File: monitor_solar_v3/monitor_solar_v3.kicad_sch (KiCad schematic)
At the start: 41 parts, among them J1 Panel, J10 GPIO, J11 Jumper, J2 ACS712, J3 Battery, J4 AMP_OUT, J5 JUMPER_PROG, J6 JUMPER_PROG, J7 PROGRAM, J9 Reg 5V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

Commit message: PCB V3 finished
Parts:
- added R15: 10k, Resistor_THT:R_Axial_DIN0207_L6.3mm_D2.5mm_P10.16mm_Horizontal, symbol Device:R
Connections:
- net +3.3V: now also R15.1
- net GPIO15: now also R15.2
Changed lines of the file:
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@@
 	)
 	(junction
+		(at 260.35 60.96)
+		(diameter 0)
+		(color 0 0 0 0)
+	)
+	(junction
 		(at 22.86 25.4)
 		(diameter 0)
@@
 	(wire
 		(pts
+			(xy 260.35 50.8) (xy 260.35 52.07)
+		)
+		(stroke
+			(width 0)
+			(type default)
+		)
+	)
+	(wire
+		(pts
 			(xy 49.53 134.62) (xy 49.53 132.08)
 		)
@@
 	(wire
 		(pts
-			(xy 238.76 60.96) (xy 234.95 60.96)
-		)
-		(stroke
-			(width 0)
-			(type default)
-		)
-	)
-	(wire
-		(pts
 			(xy 48.26 81.28) (xy 50.8 81.28)
 		)
@@
 	(wire
 		(pts
+			(xy 260.35 60.96) (xy 234.95 60.96)
+		)
+		(stroke
+			(width 0)
+			(type default)
+		)
+	)
+	(wire
+		(pts
 			(xy 196.85 25.4) (xy 199.39 25.4)
 		)
@@
 	(wire
 		(pts
+			(xy 260.35 59.69) (xy 260.35 60.96)
+		)
+		(stroke
+			(width 0)
+			(type default)
+		)
+	)
+	(wire
+		(pts
 			(xy 196.85 151.13) (xy 186.69 151.13)
 		)
@@
 	(wire
 		(pts
+			(xy 260.35 60.96) (xy 265.43 60.96)
+		)
+		(stroke
+			(width 0)
+			(type default)
+		)
+	)
+	(wire
+		(pts
 			(xy 22.86 45.72) (xy 25.4 45.72)
 		)
@@
 	(global_label "GPIO15"
 		(shape input)
-		(at 238.76 60.96 0)
+		(at 265.43 60.96 0)
 		(fields_autoplaced yes)
 		(effects
@@
 		)
 		(property "Intersheetrefs" "${INTERSHEET_REFS}"
-			(at 248.6395 60.96 0)
+			(at 275.3095 60.96 0)
 			(effects
 				(font
@@
 	)
 	(symbol
+		(lib_id "power:+3.3V")
+		(at 260.35 50.8 0)
+		(unit 1)
+		(exclude_from_sim no)
+		(in_bom yes)
+		(on_board yes)
+		(dnp no)
+		(fields_autoplaced yes)
+		(property "Reference" "#PWR034"
+			(at 260.35 54.61 0)
+			(effects
+				(font
+					(size 1.27 1.27)
+				)
+				(hide yes)
+			)
+		)
+		(property "Value" "+3.3V"
+			(at 260.35 45.72 0)
+			(effects
+				(font
+					(size 1.27 1.27)
+				)
+			)
+		)
+		(property "Footprint" ""
+			(at 260.35 50.8 0)
+			(effects
+				(font
+					(size 1.27 1.27)
+				)
+				(hide yes)
+			)
+		)
+		(property "Datasheet" ""
+			(at 260.35 50.8 0)
+			(effects
+				(font
+					(size 1.27 1.27)
+				)
+				(hide yes)
+			)
+		)
+		(property "Description" "Power symbol creates a global label with name \"+3.3V\""
+			(at 260.35 50.8 0)
+			(effects
+				(font
+					(size 1.27 1.27)
+				)
+				(hide yes)
+			)
+		)
+		(pin "1"
+		)
+		(instances
+			(project "monitor_solar_v3"
+				(path "/d4e2a079-328a-41d5-a5a0-7716b5883be5"
+					(reference "#PWR034")
+					(unit 1)
+				)
+			)
+		)
+	)
+	(symbol
 		(lib_id "power:GND")
 		(at 186.69 156.21 0)
@@
 					(unit 1)
 				)
+			)
+		)
+	)
+	(symbol
+		(lib_id "Device:R")
+		(at 260.35 55.88 0)
+		(unit 1)
+		(exclude_from_sim no)
+		(in_bom yes)
+		(on_board yes)
+		(dnp no)
+		(fields_autoplaced yes)
+		(property "Reference" "R15"
+			(at 262.89 54.6099 0)
+			(effects
+				(font
+					(size 1.27 1.27)
+				)
+				(justify left)
+			)
+		)
+		(property "Value" "10k"
+			(at 262.89 57.1499 0)
+			(effects
+				(font
+					(size 1.27 1.27)
+				)
+				(justify left)
+			)
+		)
+		(property "Footprint" "Resistor_THT:R_Axial_DIN0207_L6.3mm_D2.5mm_P10.16mm_Horizontal"
+			(at 258.572 55.88 90)
+			(effects
+				(font
+					(size 1.27 1.27)
+				)
+				(hide yes)
+			)
+		)
+		(property "Datasheet" "~"
+			(at 260.35 55.88 0)
+			(effects
+				(font
+					(size 1.27 1.27)
+				)
+				(hide yes)
+			)
+		)
+		(property "Description" "Resistor"
+			(at 260.35 55.88 0)
+			(effects
+				(font
+					(size 1.27 1.27)
+				)
+				(hide yes)
+			)
+		)
+		(pin "1"
+		)
+		(pin "2"
+		)
+		(instances
+			(project "monitor_solar_v3"
+				(path "/d4e2a079-328a-41d5-a5a0-7716b5883be5"
+					(reference "R15")
+					(unit 1)
+				)

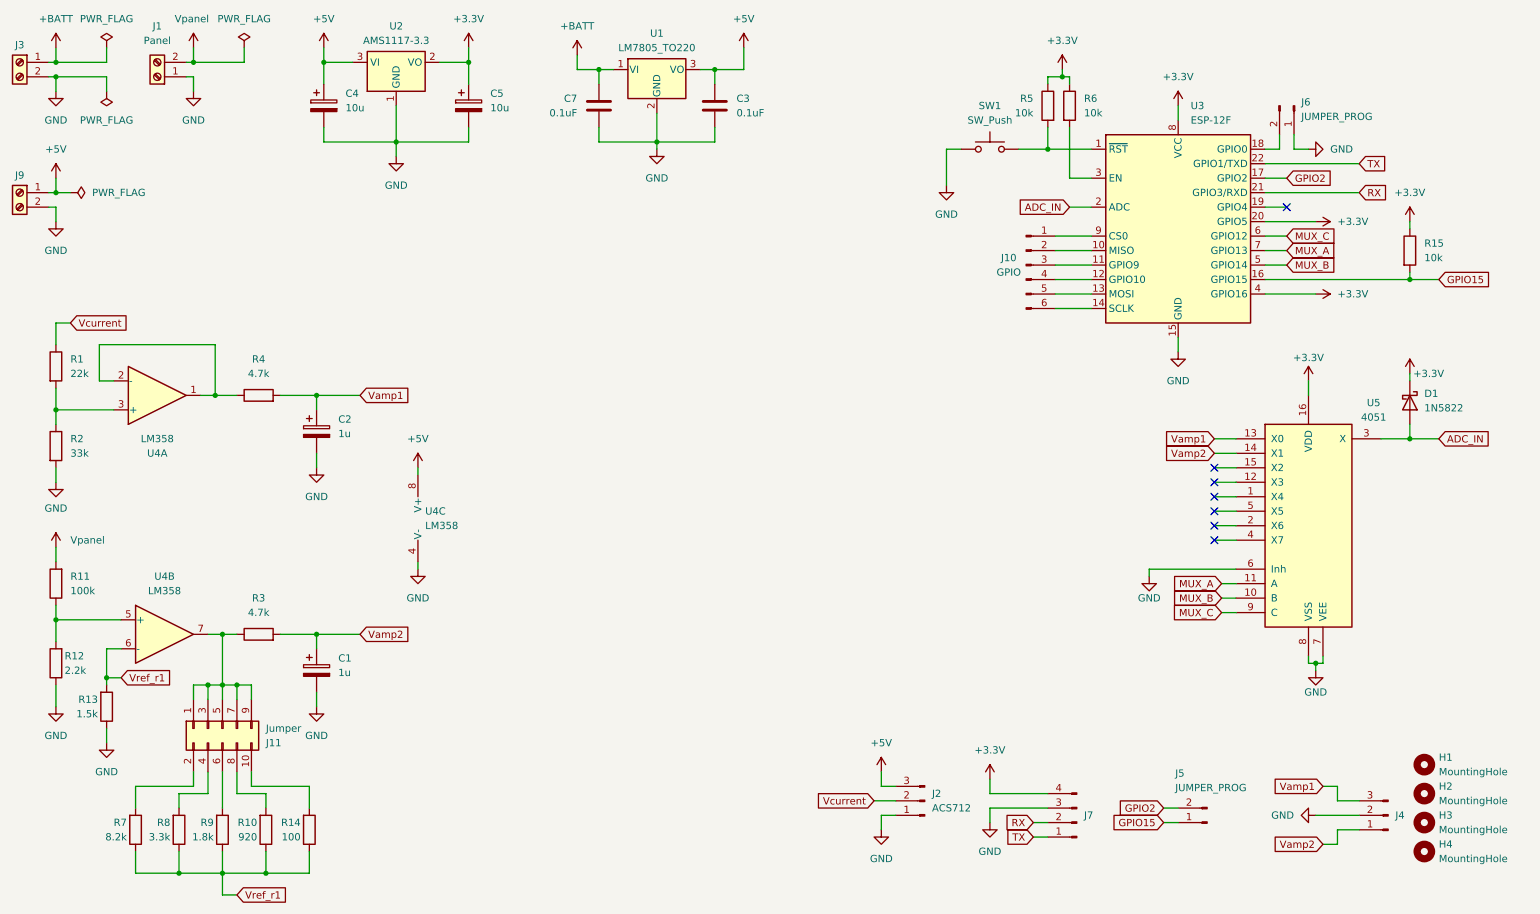
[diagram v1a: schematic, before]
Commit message: Add led for power status
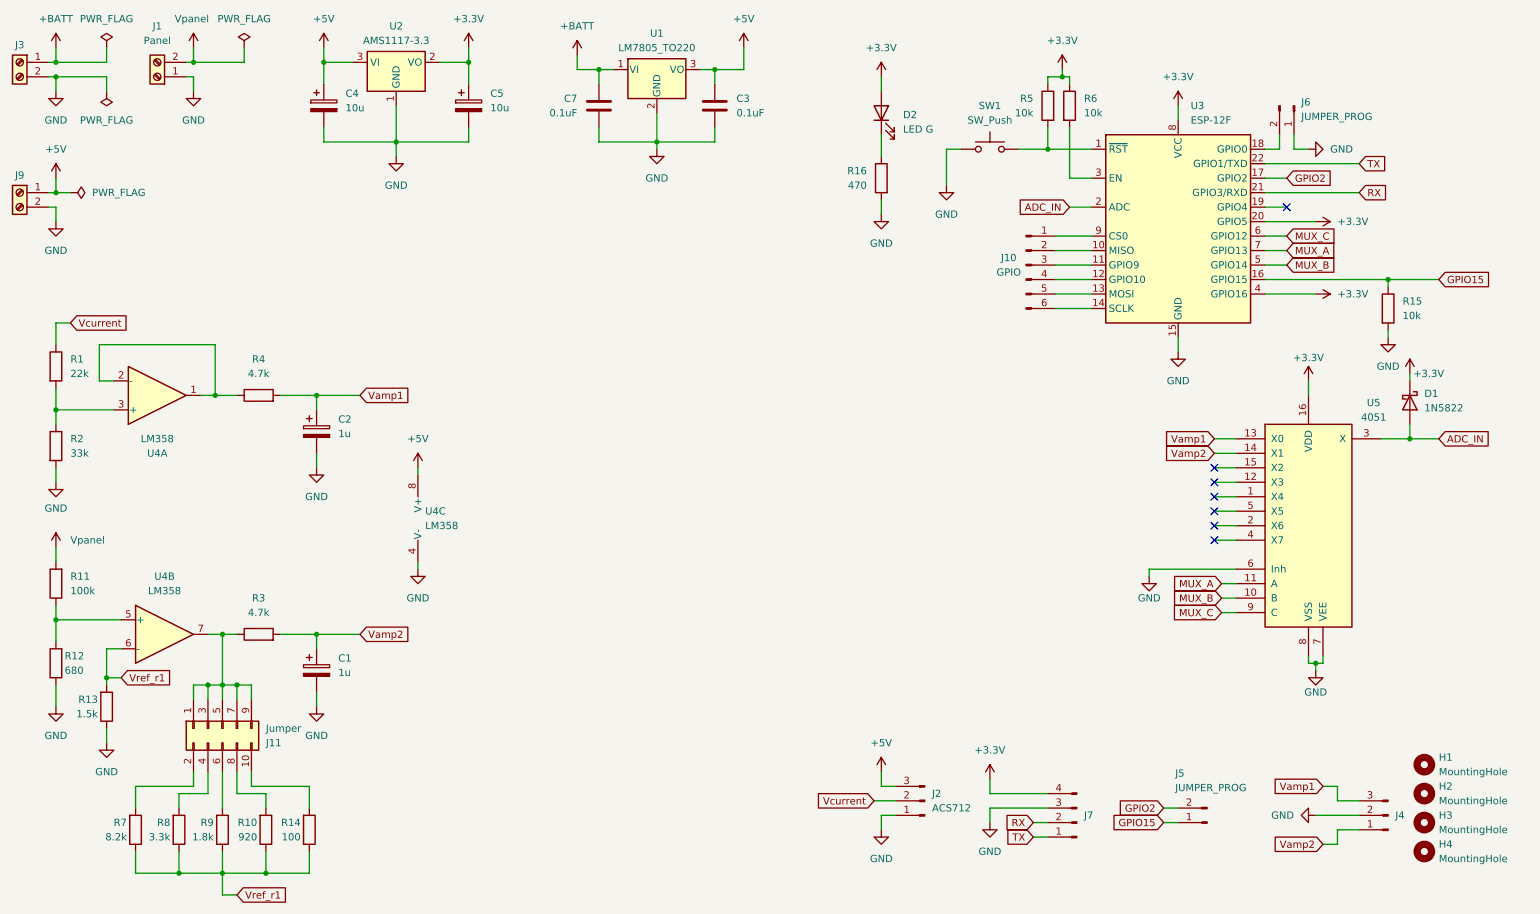
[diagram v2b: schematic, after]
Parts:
- added D2: LED G, LED_THT:LED_D3.0mm, symbol Device:LED
- added R16: 470, Resistor_THT:R_Axial_DIN0207_L6.3mm_D2.5mm_P10.16mm_Horizontal, symbol Device:R
- R12: value 2.2k -> 680
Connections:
- net +3.3V: now also D2.2 (A); no longer R15.1
- net GND: now also R15.2, R16.2
- net GPIO15: now also R15.1; no longer R15.2
- new net: D2.1 (K), R16.1
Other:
- moved on the sheet: R15

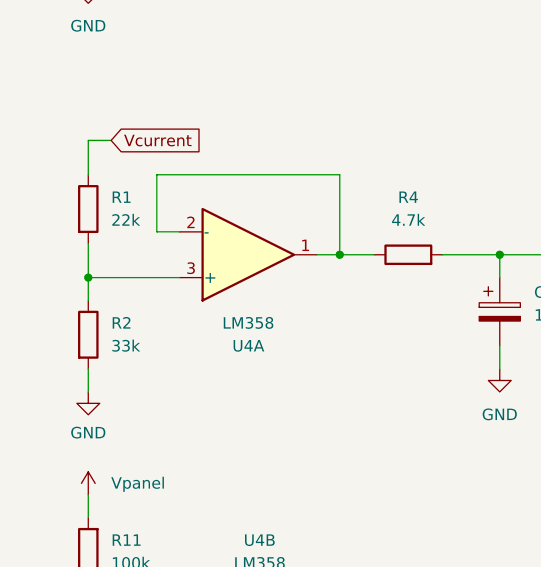
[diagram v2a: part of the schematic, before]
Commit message: Cambios en la sensibilidad de los canales. Modificar valores de resistencias en esquematico
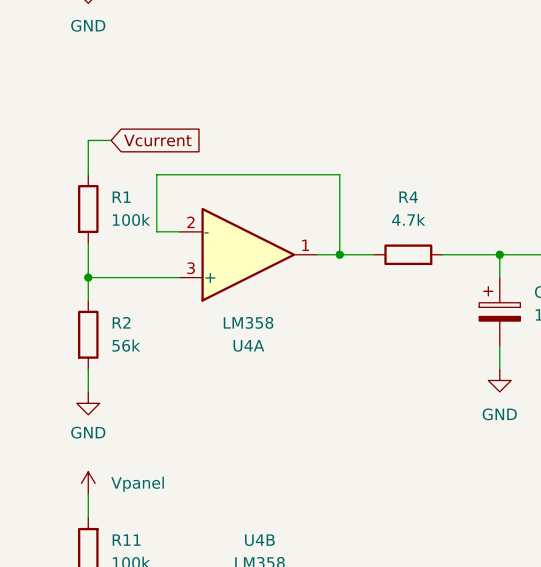
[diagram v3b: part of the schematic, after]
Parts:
- R1: value 22k -> 100k
- R2: value 33k -> 56k
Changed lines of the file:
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@@
 			)
 		)
-		(property "Value" "33k"
+		(property "Value" "56k"
 			(at 25.4 91.4399 0)
 			(effects
@@
 			)
 		)
-		(property "Value" "22k"
+		(property "Value" "100k"
 			(at 25.4 77.4699 0)
 			(effects
